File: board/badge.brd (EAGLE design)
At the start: 157.7 x 91.3 mm, 45 parts, among them IC1 STM32F030F4, IC2 UBLOX_MAX, IC3 RFM69HW, IC4 MCP1640, J2 20-0096, J3 SWD_PTH_SHROUD, X1 RADIOMETRIX-MTX2, X2 SMA-142-0701-851/861, X3 091OLED

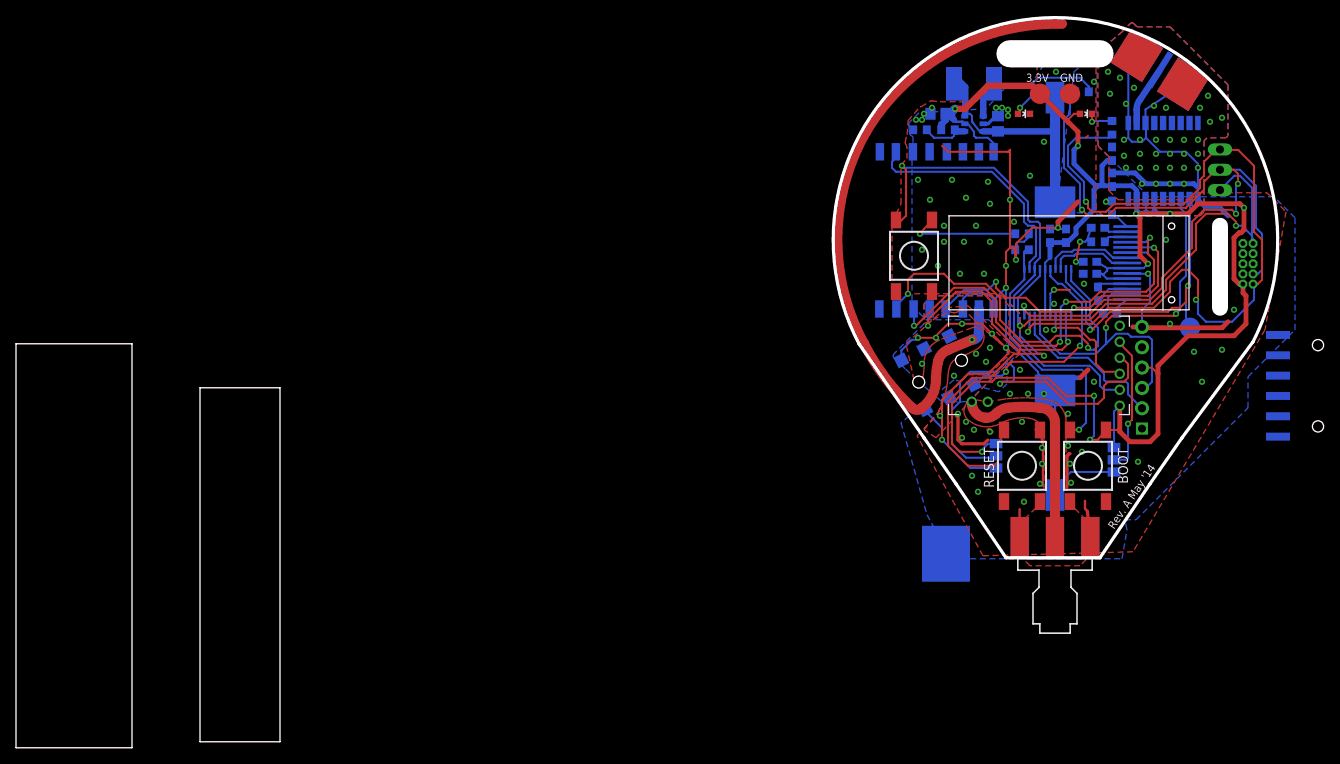
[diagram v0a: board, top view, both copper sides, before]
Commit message: Tidy up
Replaced octagonal vias with round ones
Replaced 0.381mm vias with 0.3mm
Fixed 3 airwires
Amended 20 Dimension to width 0
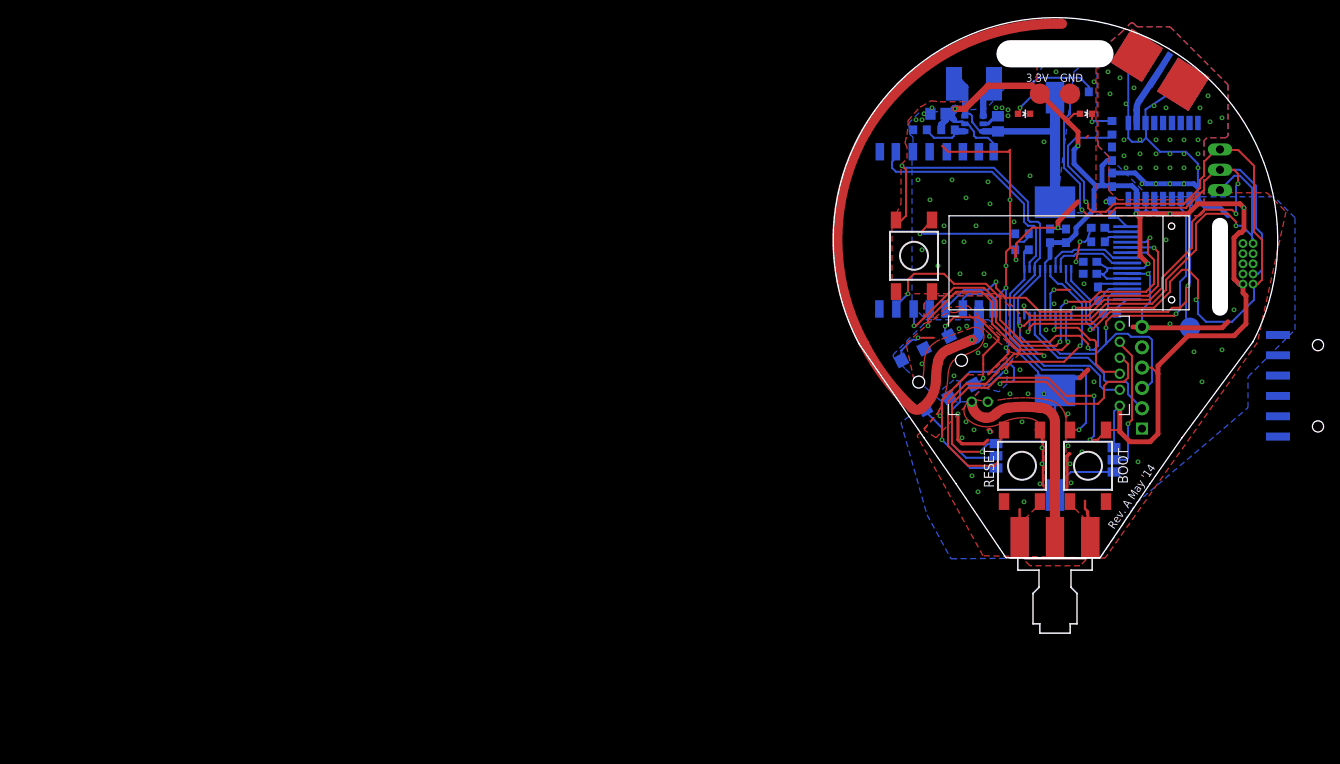
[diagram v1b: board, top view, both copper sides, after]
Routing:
- net ADC1: track 27.2 -> 44.4 mm, vias 2 -> 4
- net 0V: track 271.5 -> 258.5 mm, vias 115 -> 114
- net NRST: track 96.2 -> 96.8 mm
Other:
- board size 157.7 x 91.3 mm -> 55.6 x 67.5 mm

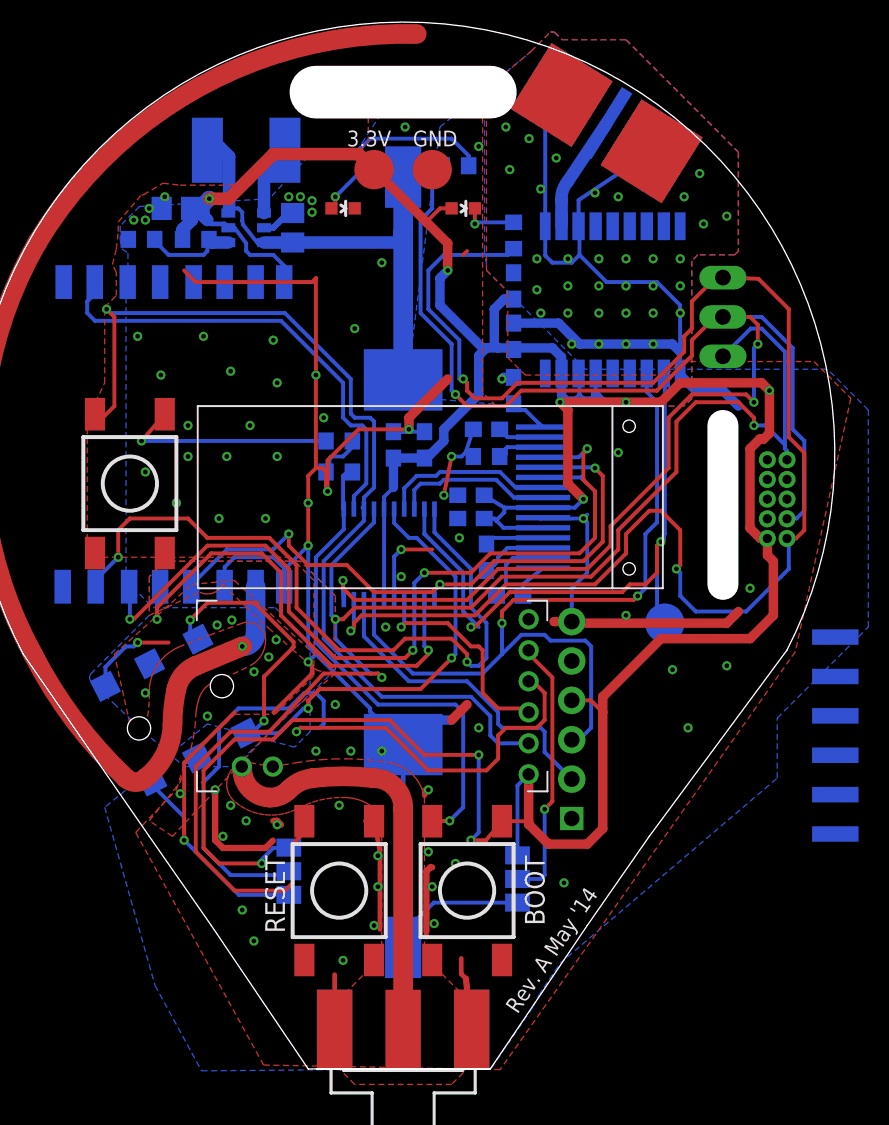
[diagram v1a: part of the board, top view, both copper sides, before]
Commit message: adding DC bias resistors
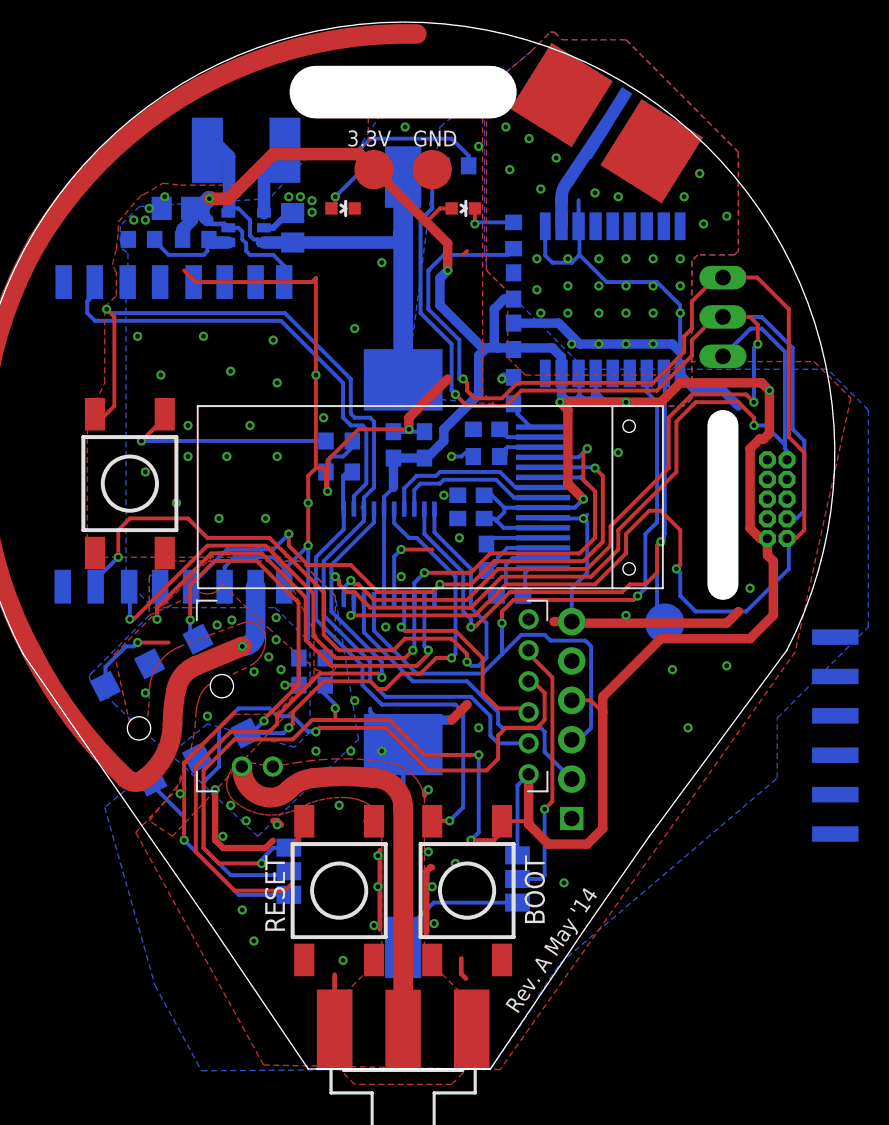
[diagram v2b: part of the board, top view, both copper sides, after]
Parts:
- added R8, R9: 10k, rcl:R0603
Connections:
- net +3V3: now also R8.2
- net 0V: now also R9.1
- net ADC1: now also R8.1, R9.2
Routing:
- net 0V: track 258.5 -> 222.4 mm, vias 114 -> 115
- net ADC1: track 44.4 -> 54.0 mm, vias 4 -> 5
- net N$18: track 48.4 -> 43.2 mm
- net +3V3: track 212.5 -> 216.2 mm, vias 9 -> 10
- net SWDAT: track 100.6 -> 99.1 mm
- net NRST: track 96.8 -> 97.8 mm
- net SWCLK: track 98.9 -> 98.3 mm
- net N$2: track 41.5 -> 40.9 mm
- net TX: track 14.2 -> 13.7 mm

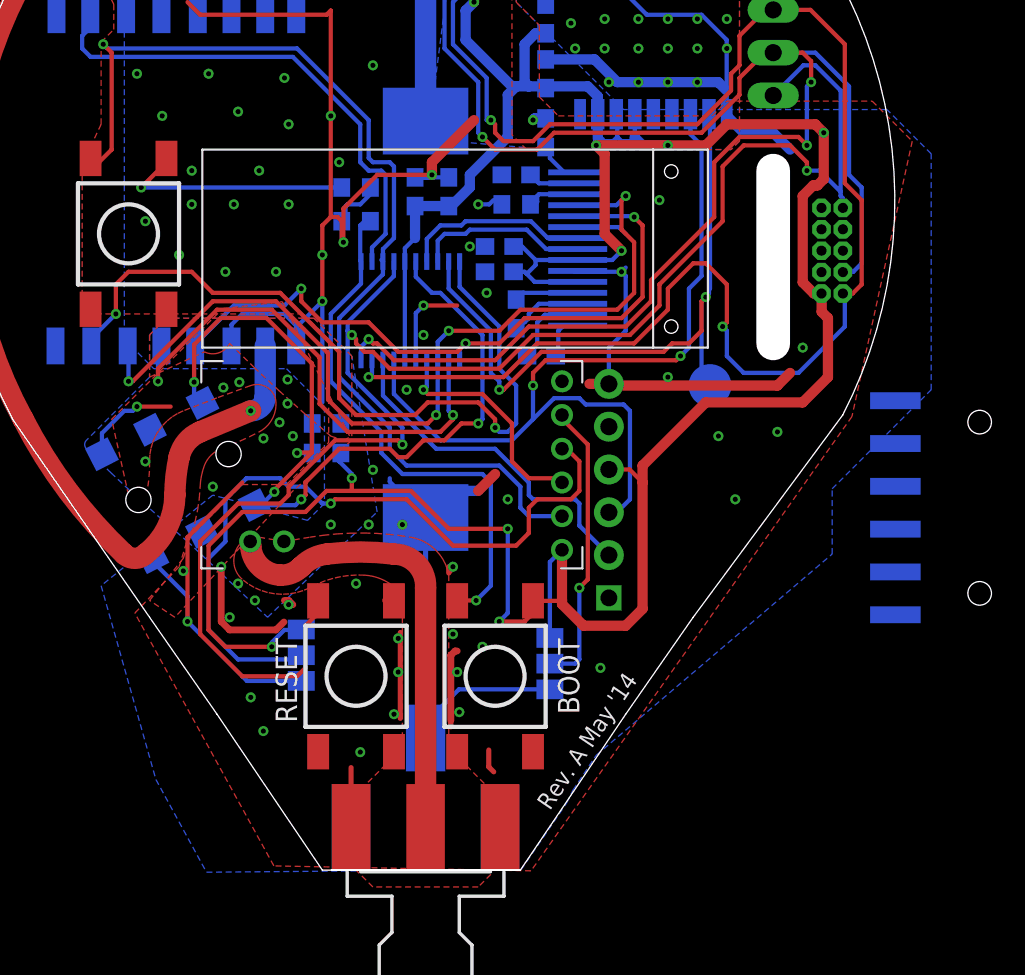
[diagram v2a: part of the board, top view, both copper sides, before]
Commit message: Tied Reset pin on GPS to VCC
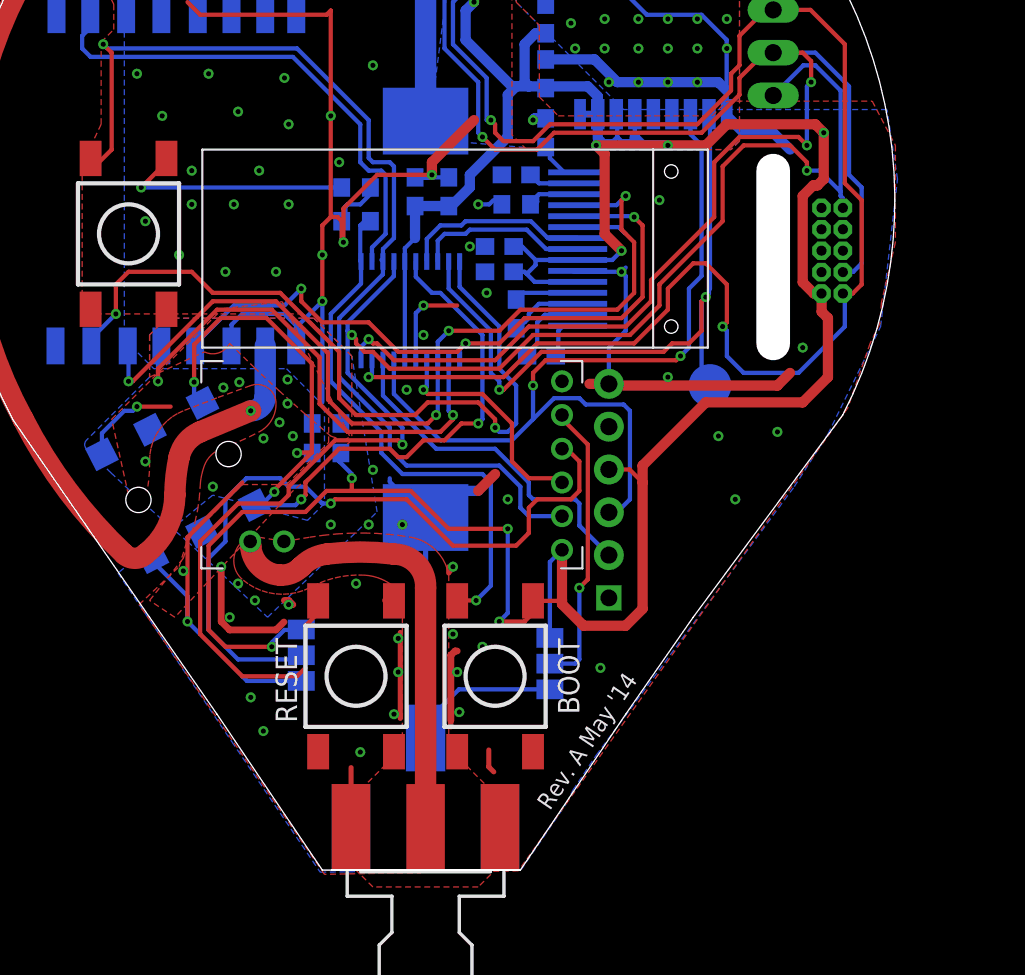
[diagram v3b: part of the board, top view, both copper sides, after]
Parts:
- removed JP2: (no value), SparkFun-Connectors:1X06-SMD
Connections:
- removed net 9_V_RESET: IC2.9_V_RESET
- net +3V3: now also IC2.9_V_RESET
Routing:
- net +3V3: track 216.2 -> 217.3 mm
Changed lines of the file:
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@@
 <?xml version="1.0" encoding="utf-8"?>
 <!DOCTYPE eagle SYSTEM "eagle.dtd">
-<eagle version="6.5.0">
+<eagle version="6.4">
 <drawing>
 <settings>
@@
 <layers>
 <layer number="1" name="Top" color="4" fill="1" visible="yes" active="yes"/>
-<layer number="2" name="Route2" color="1" fill="3" visible="no" active="yes"/>
-<layer number="3" name="Route3" color="4" fill="3" visible="no" active="yes"/>
-<layer number="4" name="Route4" color="1" fill="4" visible="no" active="yes"/>
-<layer number="5" name="Route5" color="4" fill="4" visible="no" active="yes"/>
-<layer number="6" name="Route6" color="1" fill="8" visible="no" active="yes"/>
-<layer number="7" name="Route7" color="4" fill="8" visible="no" active="yes"/>
-<layer number="8" name="Route8" color="1" fill="2" visible="no" active="yes"/>
-<layer number="9" name="Route9" color="4" fill="2" visible="no" active="yes"/>
-<layer number="10" name="Route10" color="1" fill="7" visible="no" active="yes"/>
-<layer number="11" name="Route11" color="4" fill="7" visible="no" active="yes"/>
-<layer number="12" name="Route12" color="1" fill="5" visible="no" active="yes"/>
-<layer number="13" name="Route13" color="4" fill="5" visible="no" active="yes"/>
-<layer number="14" name="Route14" color="1" fill="6" visible="no" active="yes"/>
-<layer number="15" name="Route15" color="4" fill="6" visible="no" active="yes"/>
+<layer number="2" name="Route2" color="1" fill="3" visible="yes" active="yes"/>
+<layer number="3" name="Route3" color="4" fill="3" visible="yes" active="yes"/>
+<layer number="4" name="Route4" color="1" fill="4" visible="yes" active="yes"/>
+<layer number="5" name="Route5" color="4" fill="4" visible="yes" active="yes"/>
+<layer number="6" name="Route6" color="1" fill="8" visible="yes" active="yes"/>
+<layer number="7" name="Route7" color="4" fill="8" visible="yes" active="yes"/>
+<layer number="8" name="Route8" color="1" fill="2" visible="yes" active="yes"/>
+<layer number="9" name="Route9" color="4" fill="2" visible="yes" active="yes"/>
+<layer number="10" name="Route10" color="1" fill="7" visible="yes" active="yes"/>
+<layer number="11" name="Route11" color="4" fill="7" visible="yes" active="yes"/>
+<layer number="12" name="Route12" color="1" fill="5" visible="yes" active="yes"/>
+<layer number="13" name="Route13" color="4" fill="5" visible="yes" active="yes"/>
+<layer number="14" name="Route14" color="1" fill="6" visible="yes" active="yes"/>
+<layer number="15" name="Route15" color="4" fill="6" visible="yes" active="yes"/>
 <layer number="16" name="Bottom" color="1" fill="1" visible="yes" active="yes"/>
 <layer number="17" name="Pads" color="2" fill="1" visible="yes" active="yes"/>
@@
 <layer number="37" name="tTest" color="7" fill="1" visible="yes" active="yes"/>
 <layer number="38" name="bTest" color="7" fill="1" visible="yes" active="yes"/>
-<layer number="39" name="tKeepout" color="4" fill="11" visible="no" active="yes"/>
-<layer number="40" name="bKeepout" color="1" fill="11" visible="no" active="yes"/>
-<layer number="41" name="tRestrict" color="4" fill="10" visible="no" active="yes"/>
-<layer number="42" name="bRestrict" color="1" fill="10" visible="no" active="yes"/>
-<layer number="43" name="vRestrict" color="2" fill="10" visible="no" active="yes"/>
-<layer number="44" name="Drills" color="7" fill="1" visible="no" active="yes"/>
+<layer number="39" name="tKeepout" color="4" fill="11" visible="yes" active="yes"/>
+<layer number="40" name="bKeepout" color="1" fill="11" visible="yes" active="yes"/>
+<layer number="41" name="tRestrict" color="4" fill="10" visible="yes" active="yes"/>
+<layer number="42" name="bRestrict" color="1" fill="10" visible="yes" active="yes"/>
+<layer number="43" name="vRestrict" color="2" fill="10" visible="yes" active="yes"/>
+<layer number="44" name="Drills" color="7" fill="1" visible="yes" active="yes"/>
 <layer number="45" name="Holes" color="7" fill="1" visible="yes" active="yes"/>
 <layer number="46" name="Milling" color="3" fill="1" visible="yes" active="yes"/>
@@
 </class>
 </classes>
-<designrules name="Hackvana *">
+<designrules name="Hackvana">
 <description language="de">&lt;b&gt;EAGLE Design Rules für Hackvana&lt;/b&gt;
 &lt;p&gt;
@@
 <param name="dpGapFactor" value="2.5"/>
 <param name="checkGrid" value="0"/>
-<param name="checkAngle" value="1"/>
+<param name="checkAngle" value="0"/>
 <param name="checkFont" value="1"/>
 <param name="checkRestrict" value="0"/>
@@
 </element>
 <element name="J2" library="ukhas" package="3.5MMLOWPROFILE" value="20-0096" x="12" y="37.25" smashed="yes" rot="MR153"/>
-<element name="JP2" library="SparkFun-Connectors" package="1X06-SMD" value="" x="65.5" y="35.25" rot="MR270"/>
 <element name="R8" library="rcl" package="R0603" value="10k" x="26.75" y="38.5" smashed="yes" rot="MR180"/>
 <element name="R9" library="rcl" package="R0603" value="10k" x="26.75" y="40.25" smashed="yes" rot="MR0"/>
@@
 <wire x1="19" y1="69.2" x2="19.4420375" y2="69.2" width="0.254" layer="16"/>
 <wire x1="19.4420375" y1="69.2" x2="19.530753125" y2="69.288715625" width="0.254" layer="16"/>
+<contactref element="IC2" pad="9_V_RESET"/>
+<wire x1="41.79" y1="58.6" x2="42.84" y2="58.6" width="0.4064" layer="16"/>
 </signal>
 <signal name="0V">
@@
 <vertex x="50.5" y="59.375"/>
 <vertex x="59.125" y="59.375"/>
-<vertex x="61.5" y="57"/>
-<vertex x="57.9225" y="40.6625"/>
-<vertex x="38.8825" y="13.70625"/>
-<vertex x="23.625" y="14"/>
-<vertex x="15.375" y="29"/>
+<vertex x="60.5" y="56.75"/>
+<vertex x="60.5" y="51"/>
+<vertex x="59.6725" y="47.4225"/>
+<vertex x="59.5775" y="46.1725"/>
+<vertex x="59" y="45"/>
+<vertex x="57.6725" y="41.1625"/>
+<vertex x="38.1325" y="13.70625"/>
+<vertex x="26.625" y="13.5"/>
+<vertex x="15.625" y="29.5"/>
 <vertex x="18" y="31.75"/>
 <vertex x="18.5" y="33.375"/>
@@
 <vertex x="41.375" y="18.5"/>
 <vertex x="42.75" y="20.56375"/>
-<vertex x="56.75" y="32.5"/>
-<vertex x="56.75" y="36.375"/>
-<vertex x="62.625" y="42.25"/>
-<vertex x="62.625" y="56.25"/>
+<vertex x="54.5" y="36.5"/>
+<vertex x="56.5" y="39.625"/>
+<vertex x="59.625" y="46"/>
+<vertex x="60.625" y="54.75"/>
 <vertex x="60" y="58.875"/>
 <vertex x="44.375" y="58.875"/>
@@
 <vertex x="25.625" y="34.5"/>
 <vertex x="20" y="36"/>
-<vertex x="13.375" y="30.625"/>
-<vertex x="16.625" y="19.125"/>
-<vertex x="19.625" y="13.625"/>
+<vertex x="14.375" y="31.375"/>
+<vertex x="21.125" y="21.375"/>
+<vertex x="26.375" y="13.625"/>
 <vertex x="38.30125" y="13.78375"/>
 <vertex x="40.99" y="17.72625"/>
@@
 <wire x1="37" y1="42.75" x2="37" y2="42.25" width="0.254" layer="16"/>
 </signal>
-<signal name="9_V_RESET">
-<contactref element="IC2" pad="9_V_RESET"/>
-</signal>
 <signal name="N$7">
